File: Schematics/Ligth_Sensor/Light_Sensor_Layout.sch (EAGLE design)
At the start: 7 parts, among them J1 RJ45

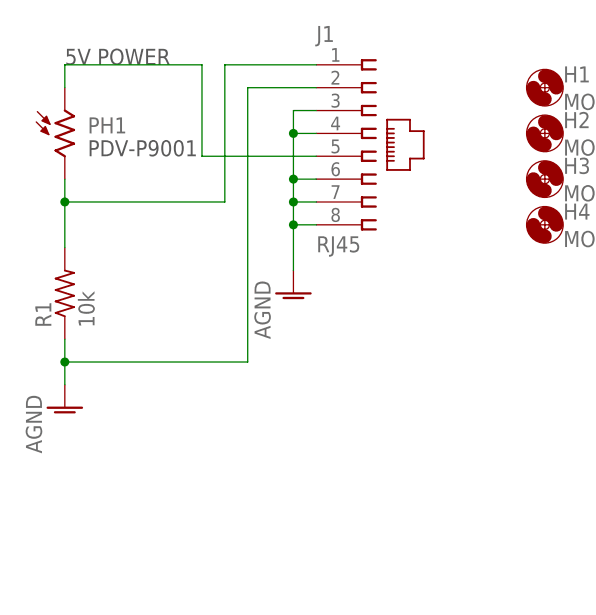
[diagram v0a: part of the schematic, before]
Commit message: Updated Sensor Module PCBs
Switched Ethernet I/O. Rerouted PCB
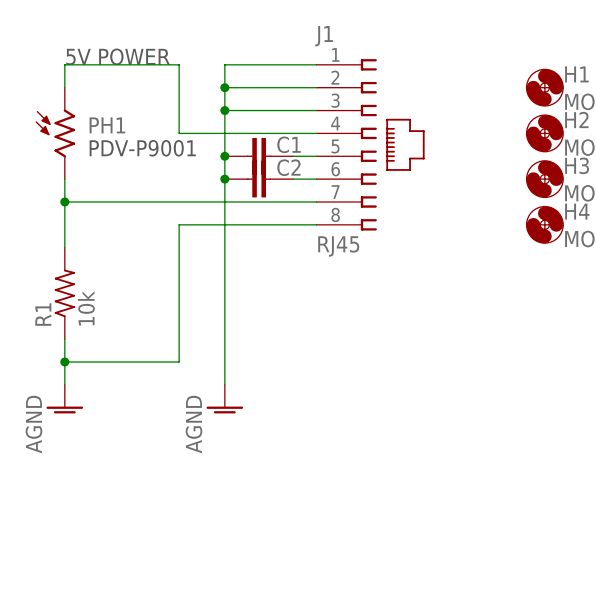
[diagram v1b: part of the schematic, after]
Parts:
- added C1, C2: (no value), rcl:C-EUC0603K
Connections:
- new net N$23: C1.2, J1.5
- new net N$24: C2.2, J1.6
- net AGND: now also C1.1, C2.1, J1.1; no longer J1.4, J1.6, J1.7
- net N$1: now also J1.4; no longer J1.5
- net N$2: now also J1.7; no longer J1.1
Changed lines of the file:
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@@
 <?xml version="1.0" encoding="utf-8"?>
 <!DOCTYPE eagle SYSTEM "eagle.dtd">
-<eagle version="6.4">
+<eagle version="6.3">
 <drawing>
 <settings>
@@
 <part name="H4" library="holes" deviceset="MOUNT-HOLE" device="2.8"/>
 <part name="FRAME1" library="frames" deviceset="FRAME_A_L" device="" value="4"/>
+<part name="C1" library="rcl" deviceset="C-EU" device="C0603K"/>
+<part name="C2" library="rcl" deviceset="C-EU" device="C0603K"/>
 </parts>
 <sheets>
@@
 <instance part="J1" gate="G$1" x="119.38" y="55.88"/>
 <instance part="AGND1" gate="VR1" x="86.36" y="25.4"/>
-<instance part="AGND2" gate="VR1" x="111.76" y="38.1"/>
+<instance part="AGND2" gate="VR1" x="104.14" y="25.4"/>
 <instance part="H1" gate="G$1" x="139.7" y="60.96"/>
 <instance part="H2" gate="G$1" x="139.7" y="55.88"/>
@@
 <attribute name="SHEET" x="218.44" y="-34.29" size="2.54" layer="94" font="vector"/>
 </instance>
+<instance part="C1" gate="G$1" x="106.68" y="53.34" smashed="yes" rot="R90">
+<attribute name="NAME" x="112.776" y="55.499" size="1.778" layer="95" rot="R180"/>
+<attribute name="VALUE" x="111.379" y="54.864" size="1.778" layer="96" rot="R90"/>
+</instance>
+<instance part="C2" gate="G$1" x="106.68" y="50.8" smashed="yes" rot="R90">
+<attribute name="NAME" x="112.776" y="52.959" size="1.778" layer="95" rot="R180"/>
+<attribute name="VALUE" x="111.379" y="52.324" size="1.778" layer="96" rot="R90"/>
+</instance>
 </instances>
 <busses>
@@
 <net name="N$1" class="0">
 <segment>
-<pinref part="J1" gate="G$1" pin="5"/>
-<wire x1="114.3" y1="53.34" x2="101.6" y2="53.34" width="0.1524" layer="91"/>
-<wire x1="101.6" y1="53.34" x2="101.6" y2="63.5" width="0.1524" layer="91"/>
-<wire x1="101.6" y1="63.5" x2="86.36" y2="63.5" width="0.1524" layer="91"/>
+<wire x1="99.06" y1="63.5" x2="86.36" y2="63.5" width="0.1524" layer="91"/>
 <pinref part="PH1" gate="G$1" pin="1"/>
 <wire x1="86.36" y1="63.5" x2="86.36" y2="60.96" width="0.1524" layer="91"/>
+<wire x1="99.06" y1="63.5" x2="99.06" y2="55.88" width="0.1524" layer="91"/>
+<pinref part="J1" gate="G$1" pin="4"/>
+<wire x1="99.06" y1="55.88" x2="114.3" y2="55.88" width="0.1524" layer="91"/>
 </segment>
 </net>
@@
 <wire x1="86.36" y1="50.8" x2="86.36" y2="48.26" width="0.1524" layer="91"/>
 <wire x1="86.36" y1="48.26" x2="86.36" y2="43.18" width="0.1524" layer="91"/>
-<wire x1="86.36" y1="48.26" x2="104.14" y2="48.26" width="0.1524" layer="91"/>
-<wire x1="104.14" y1="48.26" x2="104.14" y2="63.5" width="0.1524" layer="91"/>
+<wire x1="86.36" y1="48.26" x2="114.3" y2="48.26" width="0.1524" layer="91"/>
 <junction x="86.36" y="48.26"/>
-<pinref part="J1" gate="G$1" pin="1"/>
-<wire x1="104.14" y1="63.5" x2="114.3" y2="63.5" width="0.1524" layer="91"/>
+<pinref part="J1" gate="G$1" pin="7"/>
 </segment>
 </net>
@@
 <wire x1="86.36" y1="33.02" x2="86.36" y2="30.48" width="0.1524" layer="91"/>
 <wire x1="86.36" y1="30.48" x2="86.36" y2="27.94" width="0.1524" layer="91"/>
-<wire x1="86.36" y1="30.48" x2="106.68" y2="30.48" width="0.1524" layer="91"/>
-<wire x1="106.68" y1="30.48" x2="106.68" y2="60.96" width="0.1524" layer="91"/>
+<wire x1="86.36" y1="30.48" x2="99.06" y2="30.48" width="0.1524" layer="91"/>
 <junction x="86.36" y="30.48"/>
-<pinref part="J1" gate="G$1" pin="2"/>
-<wire x1="106.68" y1="60.96" x2="114.3" y2="60.96" width="0.1524" layer="91"/>
 <pinref part="AGND1" gate="VR1" pin="AGND"/>
+<wire x1="99.06" y1="30.48" x2="99.06" y2="45.72" width="0.1524" layer="91"/>
+<pinref part="J1" gate="G$1" pin="8"/>
+<wire x1="99.06" y1="45.72" x2="114.3" y2="45.72" width="0.1524" layer="91"/>
 </segment>
 <segment>
+<pinref part="AGND2" gate="VR1" pin="AGND"/>
+<wire x1="104.14" y1="58.42" x2="104.14" y2="53.34" width="0.1524" layer="91"/>
+<pinref part="J1" gate="G$1" pin="1"/>
+<wire x1="104.14" y1="53.34" x2="104.14" y2="50.8" width="0.1524" layer="91"/>
+<wire x1="104.14" y1="50.8" x2="104.14" y2="27.94" width="0.1524" layer="91"/>
+<wire x1="114.3" y1="63.5" x2="104.14" y2="63.5" width="0.1524" layer="91"/>
+<wire x1="104.14" y1="63.5" x2="104.14" y2="60.96" width="0.1524" layer="91"/>
+<pinref part="J1" gate="G$1" pin="2"/>
+<wire x1="104.14" y1="60.96" x2="104.14" y2="58.42" width="0.1524" layer="91"/>
+<wire x1="114.3" y1="60.96" x2="104.14" y2="60.96" width="0.1524" layer="91"/>
+<junction x="104.14" y="60.96"/>
 <pinref part="J1" gate="G$1" pin="3"/>
-<wire x1="114.3" y1="58.42" x2="111.76" y2="58.42" width="0.1524" layer="91"/>
-<pinref part="AGND2" gate="VR1" pin="AGND"/>
-<wire x1="111.76" y1="58.42" x2="111.76" y2="55.88" width="0.1524" layer="91"/>
-<pinref part="J1" gate="G$1" pin="4"/>
-<wire x1="111.76" y1="55.88" x2="111.76" y2="50.8" width="0.1524" layer="91"/>
-<wire x1="111.76" y1="50.8" x2="111.76" y2="48.26" width="0.1524" layer="91"/>
-<wire x1="111.76" y1="48.26" x2="111.76" y2="45.72" width="0.1524" layer="91"/>
-<wire x1="111.76" y1="45.72" x2="111.76" y2="40.64" width="0.1524" layer="91"/>
-<wire x1="114.3" y1="55.88" x2="111.76" y2="55.88" width="0.1524" layer="91"/>
-<junction x="111.76" y="55.88"/>
+<wire x1="114.3" y1="58.42" x2="104.14" y2="58.42" width="0.1524" layer="91"/>
+<junction x="104.14" y="58.42"/>
+<pinref part="C1" gate="G$1" pin="1"/>
+<junction x="104.14" y="53.34"/>
+<pinref part="C2" gate="G$1" pin="1"/>
+<junction x="104.14" y="50.8"/>
+</segment>
+</net>
+<net name="N$23" class="0">
+<segment>
+<pinref part="J1" gate="G$1" pin="5"/>
+<wire x1="114.3" y1="53.34" x2="111.76" y2="53.34" width="0.1524" layer="91"/>
+<pinref part="C1" gate="G$1" pin="2"/>
+</segment>
+</net>
+<net name="N$24" class="0">
+<segment>
 <pinref part="J1" gate="G$1" pin="6"/>
 <wire x1="114.3" y1="50.8" x2="111.76" y2="50.8" width="0.1524" layer="91"/>
-<junction x="111.76" y="50.8"/>
-<pinref part="J1" gate="G$1" pin="7"/>
-<wire x1="114.3" y1="48.26" x2="111.76" y2="48.26" width="0.1524" layer="91"/>
-<junction x="111.76" y="48.26"/>
-<pinref part="J1" gate="G$1" pin="8"/>
-<wire x1="114.3" y1="45.72" x2="111.76" y2="45.72" width="0.1524" layer="91"/>
-<junction x="111.76" y="45.72"/>
+<pinref part="C2" gate="G$1" pin="2"/>
 </segment>
 </net>

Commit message: Layout for final inspection
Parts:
- C1, C2: value (none) -> 0.1uF
- PH1: value VT83N2 -> VT90N2; device photo-elements:VT83N2 -> photo-elements:VT90N2
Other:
- note removed: "PDV-P9001"
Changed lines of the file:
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@@
 <?xml version="1.0" encoding="utf-8"?>
 <!DOCTYPE eagle SYSTEM "eagle.dtd">
-<eagle version="6.3">
+<eagle version="6.4">
 <drawing>
 <settings>
@@
 <grid distance="0.1" unitdist="inch" unit="inch" style="lines" multiple="1" display="no" altdistance="0.01" altunitdist="inch" altunit="inch"/>
 <layers>
-<layer number="1" name="Top" color="4" fill="1" visible="yes" active="no"/>
-<layer number="16" name="Bottom" color="1" fill="1" visible="yes" active="no"/>
-<layer number="17" name="Pads" color="2" fill="1" visible="yes" active="no"/>
-<layer number="18" name="Vias" color="2" fill="1" visible="yes" active="no"/>
-<layer number="19" name="Unrouted" color="6" fill="1" visible="yes" active="no"/>
-<layer number="20" name="Dimension" color="15" fill="1" visible="yes" active="no"/>
-<layer number="21" name="tPlace" color="7" fill="1" visible="yes" active="no"/>
-<layer number="22" name="bPlace" color="7" fill="1" visible="yes" active="no"/>
-<layer number="23" name="tOrigins" color="15" fill="1" visible="yes" active="no"/>
-<layer number="24" name="bOrigins" color="15" fill="1" visible="yes" active="no"/>
-<layer number="25" name="tNames" color="7" fill="1" visible="yes" active="no"/>
-<layer number="26" name="bNames" color="7" fill="1" visible="yes" active="no"/>
-<layer number="27" name="tValues" color="7" fill="1" visible="yes" active="no"/>
-<layer number="28" name="bValues" color="7" fill="1" visible="yes" active="no"/>
+<layer number="1" name="Top" color="4" fill="1" visible="no" active="no"/>
+<layer number="16" name="Bottom" color="1" fill="1" visible="no" active="no"/>
+<layer number="17" name="Pads" color="2" fill="1" visible="no" active="no"/>
+<layer number="18" name="Vias" color="2" fill="1" visible="no" active="no"/>
+<layer number="19" name="Unrouted" color="6" fill="1" visible="no" active="no"/>
+<layer number="20" name="Dimension" color="15" fill="1" visible="no" active="no"/>
+<layer number="21" name="tPlace" color="7" fill="1" visible="no" active="no"/>
+<layer number="22" name="bPlace" color="7" fill="1" visible="no" active="no"/>
+<layer number="23" name="tOrigins" color="15" fill="1" visible="no" active="no"/>
+<layer number="24" name="bOrigins" color="15" fill="1" visible="no" active="no"/>
+<layer number="25" name="tNames" color="7" fill="1" visible="no" active="no"/>
+<layer number="26" name="bNames" color="7" fill="1" visible="no" active="no"/>
+<layer number="27" name="tValues" color="7" fill="1" visible="no" active="no"/>
+<layer number="28" name="bValues" color="7" fill="1" visible="no" active="no"/>
 <layer number="29" name="tStop" color="7" fill="3" visible="no" active="no"/>
 <layer number="30" name="bStop" color="7" fill="6" visible="no" active="no"/>
@@
 <layer number="35" name="tGlue" color="7" fill="4" visible="no" active="no"/>
 <layer number="36" name="bGlue" color="7" fill="5" visible="no" active="no"/>
-<layer number="37" name="tTest" color="7" fill="1" visible="yes" active="no"/>
-<layer number="38" name="bTest" color="7" fill="1" visible="yes" active="no"/>
+<layer number="37" name="tTest" color="7" fill="1" visible="no" active="no"/>
+<layer number="38" name="bTest" color="7" fill="1" visible="no" active="no"/>
 <layer number="39" name="tKeepout" color="4" fill="11" visible="no" active="no"/>
 <layer number="40" name="bKeepout" color="1" fill="11" visible="no" active="no"/>
@@
 <layer number="44" name="Drills" color="7" fill="1" visible="no" active="no"/>
 <layer number="45" name="Holes" color="7" fill="1" visible="no" active="no"/>
-<layer number="46" name="Milling" color="3" fill="1" visible="yes" active="no"/>
-<layer number="47" name="Measures" color="7" fill="1" visible="yes" active="no"/>
-<layer number="48" name="Document" color="7" fill="1" visible="yes" active="no"/>
-<layer number="49" name="Reference" color="7" fill="1" visible="yes" active="no"/>
-<layer number="51" name="tDocu" color="7" fill="1" visible="yes" active="no"/>
-<layer number="52" name="bDocu" color="7" fill="1" visible="yes" active="no"/>
+<layer number="46" name="Milling" color="3" fill="1" visible="no" active="no"/>
+<layer number="47" name="Measures" color="7" fill="1" visible="no" active="no"/>
+<layer number="48" name="Document" color="7" fill="1" visible="no" active="no"/>
+<layer number="49" name="Reference" color="7" fill="1" visible="no" active="no"/>
+<layer number="51" name="tDocu" color="7" fill="1" visible="no" active="no"/>
+<layer number="52" name="bDocu" color="7" fill="1" visible="no" active="no"/>
 <layer number="91" name="Nets" color="2" fill="1" visible="yes" active="yes"/>
 <layer number="92" name="Busses" color="1" fill="1" visible="yes" active="yes"/>
@@
 </classes>
 <parts>
-<part name="PH1" library="photo-elements" deviceset="VT8" device="" technology="3N2"/>
+<part name="PH1" library="photo-elements" deviceset="VT9" device="" technology="0N2" value="VT90N2"/>
 <part name="R1" library="rcl" deviceset="R-US_" device="R1206" value="10k"/>
 <part name="J1" library="con-amp" deviceset="555167-1" device="" value="RJ45"/>
@@
 <part name="H4" library="holes" deviceset="MOUNT-HOLE" device="2.8"/>
 <part name="FRAME1" library="frames" deviceset="FRAME_A_L" device="" value="4"/>
-<part name="C1" library="rcl" deviceset="C-EU" device="C0603K"/>
-<part name="C2" library="rcl" deviceset="C-EU" device="C0603K"/>
+<part name="C1" library="rcl" deviceset="C-EU" device="C0603K" value="0.1uF"/>
+<part name="C2" library="rcl" deviceset="C-EU" device="C0603K" value="0.1uF"/>
 </parts>
 <sheets>
 <sheet>
 <plain>
-<text x="88.9" y="53.34" size="1.778" layer="97">PDV-P9001</text>
 <text x="86.36" y="63.5" size="1.778" layer="97">5V POWER</text>
 <text x="149.86" y="-20.32" size="2.54" layer="94">LIGHT SENSOR BOARD</text>
